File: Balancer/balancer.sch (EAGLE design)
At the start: 326 parts, among them Q1 BSS123W, Q10A SIR882DP-T1-GE3, Q10B SIS468DN-T1-GE3, Q11A SIR882DP-T1-GE3, Q11B SIS468DN-T1-GE3, Q12A SIR882DP-T1-GE3, Q12B SIS468DN-T1-GE3, Q1A8 SIR882DP-T1-GE3, Q1B8 SIS468DN-T1-GE3, Q2 BSS123W, Q3A SIR882DP-T1-GE3, Q3B SIS468DN-T1-GE3, Q4 MMBT3906LT1G, Q4A SIR882DP-T1-GE3, Q4B SIS468DN-T1-GE3, Q5 FDN5618P, Q5A SIR882DP-T1-GE3, Q5B SIS468DN-T1-GE3, Q6 CMPT3904E_TR_PBFREE, Q6A SIR882DP-T1-GE3, Q6B SIS468DN-T1-GE3, Q9A SIR882DP-T1-GE3, Q9B SIS468DN-T1-GE3, T10 750312504, T11 750312504, T12 750312504, T3 750312504, T4 750312504, T5 750312504, T6 750312504, T8 750312504, T9 750312504, U1 LTC3300ILXE-1PBF, U2 LTC3300ILXE-1PBF

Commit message: deleted pullups for CSBI
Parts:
- removed R47: 2k, Ilya_Teach:RES
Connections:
- removed net VREG1: R47.1
- net CSBI: no longer R47.2
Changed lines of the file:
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@@
 <part name="C4K" library="Ilya_Teach" deviceset="CAP" device="" value="1uF"/>
 <part name="C3K" library="Ilya_Teach" deviceset="CAP" device="" value="1uF"/>
-<part name="R47" library="Ilya_Teach" deviceset="RES" device="" value="2k"/>
 <part name="R20" library="Ilya_Teach" deviceset="RES" device="" value="33.2k"/>
 <part name="R19" library="Ilya_Teach" deviceset="RES" device="" value="23.7k"/>
@@
 <attribute name="VALUE" x="62.484" y="30.861" size="1.778" layer="96"/>
 </instance>
-<instance part="R47" gate="G$1" x="-25.4" y="25.4" smashed="yes" rot="R90">
-<attribute name="NAME" x="-26.8986" y="21.59" size="1.778" layer="95" rot="R90"/>
-<attribute name="VALUE" x="-22.098" y="21.59" size="1.778" layer="96" rot="R90"/>
-</instance>
 <instance part="R20" gate="G$1" x="-35.56" y="25.4" smashed="yes" rot="R90">
 <attribute name="NAME" x="-37.0586" y="21.59" size="1.778" layer="95" rot="R90"/>
@@
 <wire x1="-5.08" y1="48.26" x2="-25.4" y2="48.26" width="0.1524" layer="91"/>
 </segment>
-<segment>
-<pinref part="R47" gate="G$1" pin="2"/>
-<wire x1="-25.4" y1="30.48" x2="-25.4" y2="35.56" width="0.1524" layer="91"/>
-<label x="-25.4" y="33.02" size="1.778" layer="95"/>
-</segment>
 </net>
 <net name="SCKI" class="0">
@@
 </segment>
 </net>
-<net name="VREG1" class="0">
-<segment>
-<pinref part="R47" gate="G$1" pin="1"/>
-<wire x1="-25.4" y1="20.32" x2="-25.4" y2="15.24" width="0.1524" layer="91"/>
-<label x="-25.4" y="15.24" size="1.778" layer="95"/>
-</segment>
-</net>

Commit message: deleted C14 and moved C12 to correct position
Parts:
- removed C14: 4.7uF, rcl:C-USC1210
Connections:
- removed net C1: C12.2
- net V-: now also C12.2; no longer C14.1, C14.2
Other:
- moved on the sheet: C12
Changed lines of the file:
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@@
 <part name="C10" library="rcl" library_urn="urn:adsk.eagle:library:334" deviceset="C-US" device="C1210" package3d_urn="urn:adsk.eagle:package:23619/2" value="4.7uF"/>
 <part name="C12" library="rcl" library_urn="urn:adsk.eagle:library:334" deviceset="C-US" device="C1210" package3d_urn="urn:adsk.eagle:package:23619/2" value="4.7uF"/>
-<part name="C14" library="rcl" library_urn="urn:adsk.eagle:library:334" deviceset="C-US" device="C1210" package3d_urn="urn:adsk.eagle:package:23619/2" value="4.7uF"/>
 <part name="R1" library="Ilya_Teach" deviceset="RES" device="" value="1M"/>
 <part name="R4" library="Ilya_Teach" deviceset="RES" device="" value="1.27M"/>
@@
 <attribute name="VALUE" x="-57.404" y="54.229" size="1.778" layer="96"/>
 </instance>
-<instance part="C12" gate="G$1" x="-27.94" y="81.28" smashed="yes">
-<attribute name="NAME" x="-26.924" y="81.915" size="1.778" layer="95"/>
-<attribute name="VALUE" x="-26.924" y="77.089" size="1.778" layer="96"/>
-</instance>
-<instance part="C14" gate="G$1" x="-17.78" y="81.28" smashed="yes">
-<attribute name="NAME" x="-16.764" y="81.915" size="1.778" layer="95"/>
-<attribute name="VALUE" x="-16.764" y="77.089" size="1.778" layer="96"/>
+<instance part="C12" gate="G$1" x="53.34" y="35.56" smashed="yes">
+<attribute name="NAME" x="54.356" y="36.195" size="1.778" layer="95"/>
+<attribute name="VALUE" x="54.356" y="31.369" size="1.778" layer="96"/>
 </instance>
 <instance part="R1" gate="G$1" x="60.96" y="116.84" smashed="yes" rot="R90">
@@
 </segment>
 <segment>
-<wire x1="-17.78" y1="76.2" x2="-17.78" y2="73.66" width="0.1524" layer="91"/>
-<label x="-17.78" y="73.66" size="1.778" layer="95"/>
-<pinref part="C14" gate="G$1" pin="2"/>
-</segment>
-<segment>
 <pinref part="R19" gate="G$1" pin="1"/>
 <wire x1="-45.72" y1="20.32" x2="-45.72" y2="17.78" width="0.1524" layer="91"/>
@@
 <pinref part="C3K" gate="G$1" pin="2"/>
 <pinref part="U1" gate="A" pin="C2"/>
-<wire x1="60.96" y1="30.48" x2="50.8" y2="30.48" width="0.1524" layer="91"/>
+<wire x1="60.96" y1="30.48" x2="53.34" y2="30.48" width="0.1524" layer="91"/>
+<wire x1="53.34" y1="30.48" x2="50.8" y2="30.48" width="0.1524" layer="91"/>
 <wire x1="50.8" y1="30.48" x2="40.64" y2="30.48" width="0.1524" layer="91"/>
 <wire x1="50.8" y1="35.56" x2="50.8" y2="30.48" width="0.1524" layer="91"/>
@@
 <junction x="40.64" y="30.48"/>
 <junction x="10.16" y="30.48"/>
-</segment>
-<segment>
-<label x="-17.78" y="88.9" size="1.778" layer="95"/>
-<pinref part="C14" gate="G$1" pin="1"/>
-<wire x1="-17.78" y1="83.82" x2="-17.78" y2="91.44" width="0.1524" layer="91"/>
+<pinref part="C12" gate="G$1" pin="2"/>
+<junction x="53.34" y="30.48"/>
 </segment>
 <segment>
@@
 <segment>
 <pinref part="U1" gate="A" pin="C3"/>
-<wire x1="40.64" y1="38.1" x2="60.96" y2="38.1" width="0.1524" layer="91"/>
+<wire x1="40.64" y1="38.1" x2="53.34" y2="38.1" width="0.1524" layer="91"/>
 <pinref part="C4K" gate="G$1" pin="2"/>
 <junction x="60.96" y="38.1"/>
 <pinref part="C3K" gate="G$1" pin="1"/>
 <label x="40.64" y="38.1" size="1.778" layer="95"/>
-</segment>
-<segment>
-<label x="-27.94" y="88.9" size="1.778" layer="95"/>
 <pinref part="C12" gate="G$1" pin="1"/>
-<wire x1="-27.94" y1="83.82" x2="-27.94" y2="91.44" width="0.1524" layer="91"/>
+<wire x1="53.34" y1="38.1" x2="60.96" y2="38.1" width="0.1524" layer="91"/>
+<junction x="53.34" y="38.1"/>
 </segment>
 <segment>
@@
 </segment>
 </net>
-<net name="C1" class="0">
-<segment>
-<wire x1="-27.94" y1="76.2" x2="-27.94" y2="73.66" width="0.1524" layer="91"/>
-<label x="-27.94" y="73.66" size="1.778" layer="95"/>
-<pinref part="C12" gate="G$1" pin="2"/>
-</segment>
-</net>

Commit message: removed one lowpass resistor, did schematic check
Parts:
- removed E10, E2, E3, E9: 2501-2-00-80-00-00-07-0, Turret:2501-2-00-80-00-00-07-0
- removed F7, F8: 01530008Z, 01530008Z:01530008Z
- removed R2K: 100, rcl:R-US_R0805
- added E11, E12, E13, E14: 2501-2-00-80-00-00-07-0, Turret:2501-2-00-80-00-00-07-0
- added F10, F15: 01530008Z, 01530008Z:01530008Z
- renumbered F1 to F12, F2 to F11, R2 to R6
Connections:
- removed net N$94: C3M.1, R2K.2
- net C0_F: now also C3M.1
- net C10: now also E12.1, F10.1; no longer E4.1, F3.1
- net C11: now also E13.1; no longer E6.1
- net C12: now also E14.1; no longer E5.1
- net C3: now also E4.1, F3.2; no longer E10.1, F8.2
- net C4: now also E5.1, F4.1; no longer E2.1, F7.1
- net C5: now also E6.1, F5.2; no longer E9.1, F6.2
- net C6: now also E7.1, F6.1; no longer E3.1, F5.1
- net C9: now also E11.1, F9.2; no longer E7.1, F4.2
- net N$18: now also F10.2; no longer F3.2
- net N$22: now also F9.1; no longer F4.1
- net N$23: now also F6.2; no longer F5.2
- net N$25: now also F5.1; no longer F6.1
- net N$26: now also F4.2; no longer F7.2
- net N$28: now also F3.1; no longer F8.1
- net N$30: now also F15.2; no longer F9.2
- net V-: now also F15.1; no longer F9.1, R2K.1
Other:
- moved on the sheet: D4, E4, E5, E6, E7, F3, F4, F5, F6, F9

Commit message: update1
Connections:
- removed net CTRL: U1.CTRL
- net V-: now also U1.CTRL
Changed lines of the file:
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@@
 <part name="R13K" library="rcl" library_urn="urn:adsk.eagle:library:334" deviceset="R-US_" device="R0805" package3d_urn="urn:adsk.eagle:package:23553/2" value="100"/>
 <part name="C13M" library="Ilya_Teach" deviceset="CAP" device="" value="10nF"/>
-<part name="JP1" library="Connector" library_urn="urn:adsk.eagle:library:16378166" deviceset="PINHD-1X4" device="" package3d_urn="urn:adsk.eagle:package:47493674/1"/>
+<part name="JP1" library="Connector" library_urn="urn:adsk.eagle:library:16378166" deviceset="PINHD-1X4" device="" package3d_urn="urn:adsk.eagle:package:51802636/2"/>
 </parts>
 <sheets>
@@
 <segment>
 <pinref part="JP1" gate="A" pin="4"/>
-<wire x1="-20.32" y1="50.8" x2="-25.4" y2="50.8" width="0.1524" layer="91"/>
 <label x="-22.86" y="50.8" size="1.778" layer="95"/>
+<pinref part="U1" gate="A" pin="CTRL"/>
+<wire x1="-5.08" y1="50.8" x2="-25.4" y2="50.8" width="0.1524" layer="91"/>
 </segment>
 </net>
@@
 </segment>
 </net>
-<net name="CTRL" class="0">
-<segment>
-<pinref part="U1" gate="A" pin="CTRL"/>
-<wire x1="-5.08" y1="50.8" x2="-10.16" y2="50.8" width="0.1524" layer="91"/>
-<label x="-7.62" y="50.8" size="1.778" layer="95"/>
-</segment>
-</net>

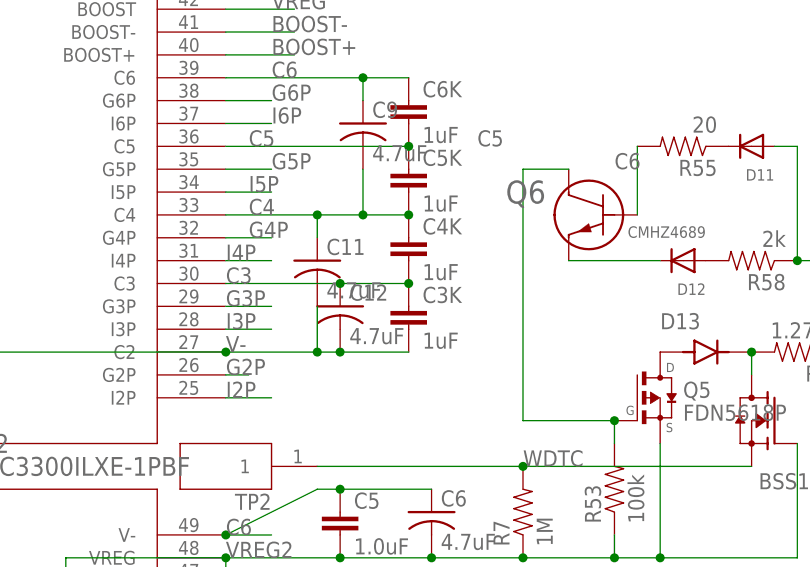
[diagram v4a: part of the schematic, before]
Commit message: changed layout
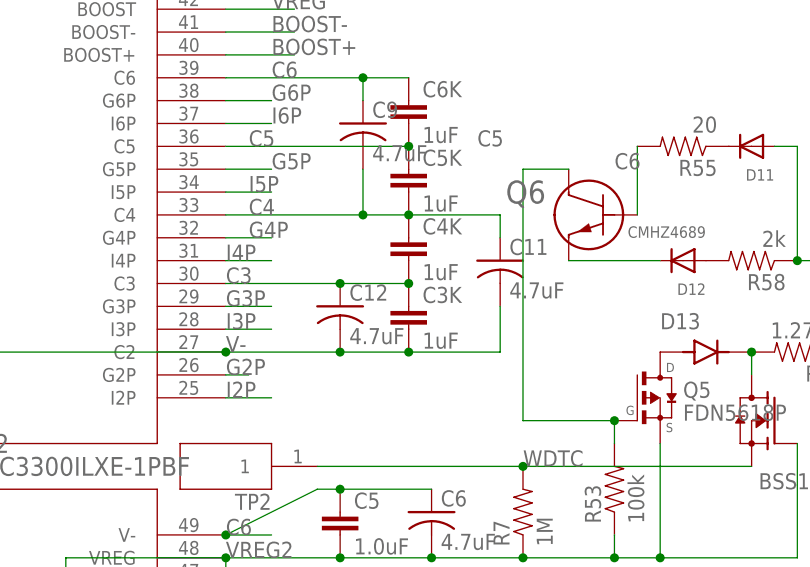
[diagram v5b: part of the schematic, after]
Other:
- moved on the sheet: C11
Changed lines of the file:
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@@
 <attribute name="VALUE" x="56.896" y="51.689" size="1.778" layer="96"/>
 </instance>
-<instance part="C11" gate="G$1" x="50.8" y="40.64" smashed="yes">
-<attribute name="NAME" x="51.816" y="41.275" size="1.778" layer="95"/>
-<attribute name="VALUE" x="51.816" y="36.449" size="1.778" layer="96"/>
+<instance part="C11" gate="G$1" x="71.12" y="40.64" smashed="yes">
+<attribute name="NAME" x="72.136" y="41.275" size="1.778" layer="95"/>
+<attribute name="VALUE" x="72.136" y="36.449" size="1.778" layer="96"/>
 </instance>
 <instance part="C10" gate="G$1" x="-58.42" y="58.42" smashed="yes">
@@
 <pinref part="C4K" gate="G$1" pin="1"/>
 <junction x="60.96" y="45.72"/>
-<wire x1="55.88" y1="45.72" x2="50.8" y2="45.72" width="0.1524" layer="91"/>
-<wire x1="50.8" y1="45.72" x2="40.64" y2="45.72" width="0.1524" layer="91"/>
+<wire x1="55.88" y1="45.72" x2="40.64" y2="45.72" width="0.1524" layer="91"/>
 <wire x1="55.88" y1="50.8" x2="55.88" y2="45.72" width="0.1524" layer="91"/>
 <junction x="55.88" y="45.72"/>
@@
 <pinref part="C9" gate="G$1" pin="2"/>
 <pinref part="C11" gate="G$1" pin="1"/>
-<wire x1="50.8" y1="43.18" x2="50.8" y2="45.72" width="0.1524" layer="91"/>
-<junction x="50.8" y="45.72"/>
+<wire x1="71.12" y1="43.18" x2="71.12" y2="45.72" width="0.1524" layer="91"/>
+<wire x1="71.12" y1="45.72" x2="60.96" y2="45.72" width="0.1524" layer="91"/>
 </segment>
 <segment>
@@
 <pinref part="U1" gate="A" pin="C2"/>
 <wire x1="60.96" y1="30.48" x2="53.34" y2="30.48" width="0.1524" layer="91"/>
-<wire x1="53.34" y1="30.48" x2="50.8" y2="30.48" width="0.1524" layer="91"/>
-<wire x1="50.8" y1="30.48" x2="40.64" y2="30.48" width="0.1524" layer="91"/>
-<wire x1="50.8" y1="35.56" x2="50.8" y2="30.48" width="0.1524" layer="91"/>
-<junction x="50.8" y="30.48"/>
+<wire x1="53.34" y1="30.48" x2="40.64" y2="30.48" width="0.1524" layer="91"/>
 <label x="40.64" y="30.48" size="1.778" layer="95"/>
-<pinref part="C11" gate="G$1" pin="2"/>
 <pinref part="U1" gate="A" pin="V-_2"/>
 <wire x1="-5.08" y1="35.56" x2="-10.16" y2="35.56" width="0.1524" layer="91"/>
@@
 <pinref part="C12" gate="G$1" pin="2"/>
 <junction x="53.34" y="30.48"/>
-</segment>
-<segment>
+<pinref part="C11" gate="G$1" pin="2"/>
+<wire x1="71.12" y1="35.56" x2="71.12" y2="30.48" width="0.1524" layer="91"/>
+<wire x1="71.12" y1="30.48" x2="60.96" y2="30.48" width="0.1524" layer="91"/>
+<junction x="60.96" y="30.48"/>
+</segment>
+<segment>

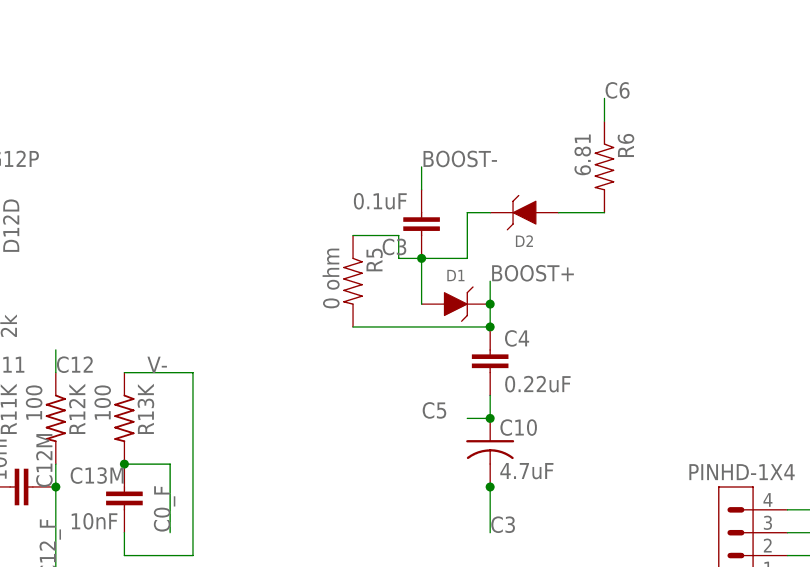
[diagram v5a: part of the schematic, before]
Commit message: removed R5 & placed all component on PCB
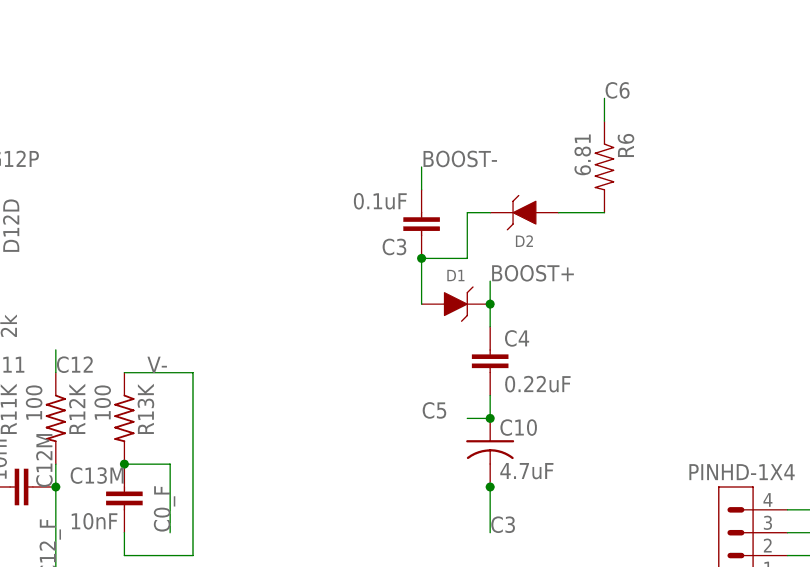
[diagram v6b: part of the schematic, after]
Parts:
- removed R5: 0 ohm, Ilya_Teach:RES
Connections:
- net BOOST+: no longer R5.2
- net N$1: no longer R5.1
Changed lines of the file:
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@@
 <part name="D2" library="DO-214AA" deviceset="WE-TVSP_DO-214AA_600W_UNI" device=""/>
 <part name="R6" library="Ilya_Teach" deviceset="RES" device="" value="6.81"/>
-<part name="R5" library="Ilya_Teach" deviceset="RES" device="" value="0 ohm"/>
 <part name="D10" library="CMOD6263" deviceset="1N4448HWT-7" device=""/>
 <part name="Q4" library="MMBT3906LT1G" deviceset="MMBT3906LT1G" device=""/>
@@
 <attribute name="VALUE" x="-49.022" y="92.71" size="1.778" layer="96" rot="R270"/>
 </instance>
-<instance part="R5" gate="G$1" x="-73.66" y="76.2" smashed="yes" rot="R270">
-<attribute name="NAME" x="-72.1614" y="80.01" size="1.778" layer="95" rot="R270"/>
-<attribute name="VALUE" x="-76.962" y="80.01" size="1.778" layer="96" rot="R270"/>
-</instance>
 <instance part="D10" gate="G$1" x="81.28" y="147.32" smashed="yes" rot="R270">
 <attribute name="NAME" x="83.82" y="152.4" size="1.778" layer="95" rot="R270"/>
@@
 <wire x1="-58.42" y1="73.66" x2="-58.42" y2="76.2" width="0.1524" layer="91"/>
 <junction x="-58.42" y="73.66"/>
-<pinref part="R5" gate="G$1" pin="2"/>
-<wire x1="-73.66" y1="71.12" x2="-58.42" y2="71.12" width="0.1524" layer="91"/>
-<junction x="-58.42" y="71.12"/>
 </segment>
 </net>
@@
 <wire x1="-60.96" y1="78.74" x2="-66.04" y2="78.74" width="0.1524" layer="91"/>
 <junction x="-66.04" y="78.74"/>
-<pinref part="R5" gate="G$1" pin="1"/>
-<wire x1="-73.66" y1="81.28" x2="-68.58" y2="81.28" width="0.1524" layer="91"/>
-<wire x1="-68.58" y1="81.28" x2="-68.58" y2="78.74" width="0.1524" layer="91"/>
-<wire x1="-68.58" y1="78.74" x2="-66.04" y2="78.74" width="0.1524" layer="91"/>
-</segment>
-</net>
+</segment>
+</net>

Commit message: merged C8 and C6
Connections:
- removed net C8: C9A.2, C9B.2, C9G.2, D9C.A, D9E.P$1, D9E.P$2, R8K.1, R9J.1, RS9A.1
- net C6: now also C9A.2, C9B.2, C9G.2, D9C.A, D9E.P$1, D9E.P$2, R8K.1, R9J.1, RS9A.1
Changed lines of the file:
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@@
 <label x="-175.26" y="66.04" size="1.778" layer="95"/>
+</segment>
+<segment>
+<pinref part="D9E" gate="G$1" pin="P$1"/>
+<pinref part="D9E" gate="G$1" pin="P$2"/>
+<wire x1="-264.16" y1="330.2" x2="-259.08" y2="330.2" width="0.1524" layer="91"/>
+<wire x1="-264.16" y1="330.2" x2="-264.16" y2="320.04" width="0.1524" layer="91"/>
+<junction x="-264.16" y="330.2"/>
+<wire x1="-264.16" y1="320.04" x2="-254" y2="320.04" width="0.1524" layer="91"/>
+<pinref part="C9B" gate="G$1" pin="2"/>
+<pinref part="C9A" gate="G$1" pin="2"/>
+<wire x1="-243.84" y1="358.14" x2="-254" y2="358.14" width="0.1524" layer="91"/>
+<wire x1="-254" y1="320.04" x2="-254" y2="332.74" width="0.1524" layer="91"/>
+<junction x="-254" y="358.14"/>
+<pinref part="D9C" gate="G$1" pin="A"/>
+<wire x1="-254" y1="332.74" x2="-254" y2="358.14" width="0.1524" layer="91"/>
+<wire x1="-248.92" y1="332.74" x2="-254" y2="332.74" width="0.1524" layer="91"/>
+<junction x="-254" y="332.74"/>
+<pinref part="C9G" gate="G$1" pin="2"/>
+<wire x1="-228.6" y1="320.04" x2="-254" y2="320.04" width="0.1524" layer="91"/>
+<junction x="-254" y="320.04"/>
+<pinref part="RS9A" gate="G$1" pin="1"/>
+<wire x1="-195.58" y1="320.04" x2="-228.6" y2="320.04" width="0.1524" layer="91"/>
+<junction x="-228.6" y="320.04"/>
+<label x="-264.16" y="320.04" size="1.778" layer="95"/>
+</segment>
+<segment>
+<pinref part="R9J" gate="G$1" pin="1"/>
+<wire x1="-137.16" y1="68.58" x2="-137.16" y2="66.04" width="0.1524" layer="91"/>
+<label x="-137.16" y="66.04" size="1.778" layer="95"/>
+<pinref part="R8K" gate="G$1" pin="1"/>
 </segment>
 </net>
@@
 </segment>
 </net>
-<net name="C8" class="0">
-<segment>
-<pinref part="D9E" gate="G$1" pin="P$1"/>
-<pinref part="D9E" gate="G$1" pin="P$2"/>
-<wire x1="-264.16" y1="330.2" x2="-259.08" y2="330.2" width="0.1524" layer="91"/>
-<wire x1="-264.16" y1="330.2" x2="-264.16" y2="320.04" width="0.1524" layer="91"/>
-<junction x="-264.16" y="330.2"/>
-<wire x1="-264.16" y1="320.04" x2="-254" y2="320.04" width="0.1524" layer="91"/>
-<pinref part="C9B" gate="G$1" pin="2"/>
-<pinref part="C9A" gate="G$1" pin="2"/>
-<wire x1="-243.84" y1="358.14" x2="-254" y2="358.14" width="0.1524" layer="91"/>
-<wire x1="-254" y1="320.04" x2="-254" y2="332.74" width="0.1524" layer="91"/>
-<junction x="-254" y="358.14"/>
-<pinref part="D9C" gate="G$1" pin="A"/>
-<wire x1="-254" y1="332.74" x2="-254" y2="358.14" width="0.1524" layer="91"/>
-<wire x1="-248.92" y1="332.74" x2="-254" y2="332.74" width="0.1524" layer="91"/>
-<junction x="-254" y="332.74"/>
-<pinref part="C9G" gate="G$1" pin="2"/>
-<wire x1="-228.6" y1="320.04" x2="-254" y2="320.04" width="0.1524" layer="91"/>
-<junction x="-254" y="320.04"/>
-<pinref part="RS9A" gate="G$1" pin="1"/>
-<wire x1="-195.58" y1="320.04" x2="-228.6" y2="320.04" width="0.1524" layer="91"/>
-<junction x="-228.6" y="320.04"/>
-<label x="-264.16" y="320.04" size="1.778" layer="95"/>
-</segment>
-<segment>
-<pinref part="R9J" gate="G$1" pin="1"/>
-<wire x1="-137.16" y1="68.58" x2="-137.16" y2="66.04" width="0.1524" layer="91"/>
-<label x="-137.16" y="66.04" size="1.778" layer="95"/>
-<pinref part="R8K" gate="G$1" pin="1"/>
-</segment>
-</net>
